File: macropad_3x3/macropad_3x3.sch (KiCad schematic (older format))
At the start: 36 parts, among them Q1 2N7002, U1 TRRS

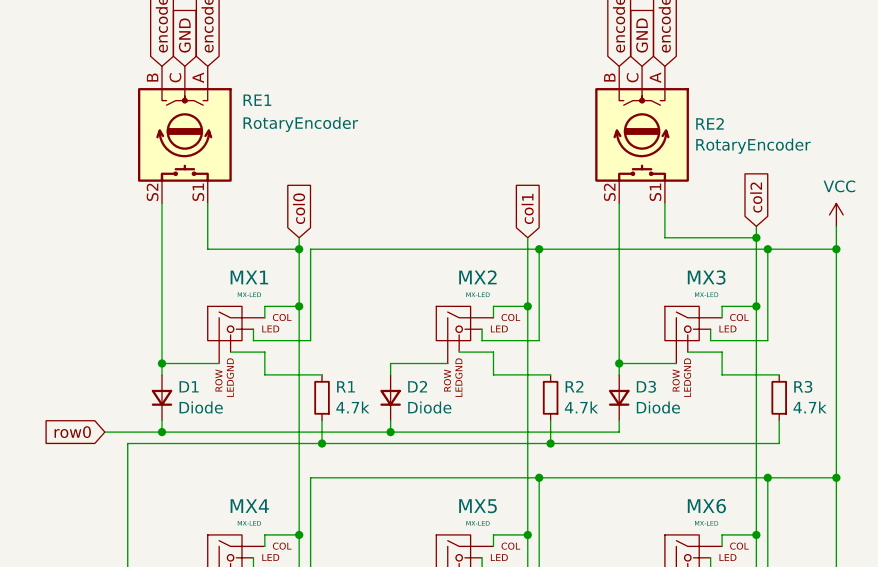
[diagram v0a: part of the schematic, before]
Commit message: 3x3 macropad v2
Updated the 3x3 macropad project to fix the issue with the rotary encoders causing the top corners to always be bridged. Slightly moved the TRRS jack further from the top right switch to give a bit more clearance for the rotary encoder pins.
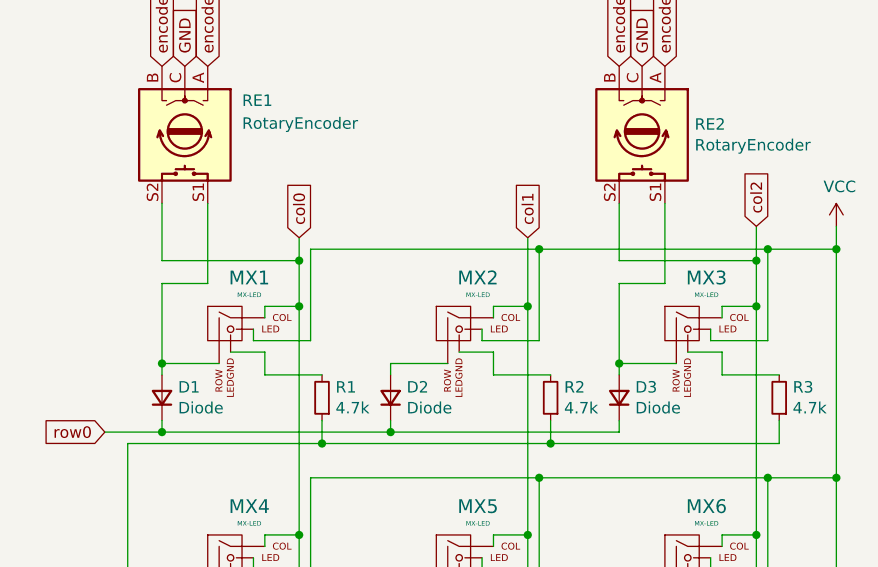
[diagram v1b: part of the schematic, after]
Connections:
- net col0: now also RE1.S2; no longer RE1.S1
- net col2: now also RE2.S2; no longer RE2.S1
- net at D1.2 (A), MX1.2 (ROW): now also RE1.S1; no longer RE1.S2
- net at D3.2 (A), MX3.2 (ROW): now also RE2.S1; no longer RE2.S2
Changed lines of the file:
@@
 	-1   0    0    1
 $EndComp
-Wire Wire Line
-	4250 2000 4250 2700
-Connection ~ 4250 2700
-Wire Wire Line
-	6450 2000 6450 2150
-Wire Wire Line
-	6250 2000 6250 2700
-Connection ~ 6250 2700
 $Comp
 L power:VCC #PWR0111
@@
 Connection ~ 4850 2450
 Wire Wire Line
-	6850 2100 6850 2150
-Wire Wire Line
 	6700 3450 6850 3450
 Wire Wire Line
@@
 	6850 2450 6850 3450
 Connection ~ 6850 2450
-Connection ~ 6850 2150
-Wire Wire Line
-	6850 2150 6850 2450
-Wire Wire Line
-	6450 2150 6850 2150
 Wire Wire Line
 	7200 2100 7200 2200
@@
 Wire Wire Line
 	5250 3000 6250 3000
-Wire Wire Line
-	4450 2000 4450 2200
-Wire Wire Line
-	4850 2200 4850 2450
-Wire Wire Line
-	4850 2150 4850 2200
-Connection ~ 4850 2200
-Wire Wire Line
-	4850 2200 4450 2200
 Wire Wire Line
 	4250 4000 5250 4000
@@
 	1    0    0    -1
 $EndComp
+Wire Wire Line
+	4850 2150 4850 2250
+Wire Wire Line
+	4250 2000 4250 2250
+Wire Wire Line
+	4250 2250 4850 2250
+Connection ~ 4850 2250
+Wire Wire Line
+	4850 2250 4850 2450
+Wire Wire Line
+	4450 2000 4450 2350
+Wire Wire Line
+	4450 2350 4250 2350
+Wire Wire Line
+	4250 2350 4250 2700
+Connection ~ 4250 2700
+Wire Wire Line
+	6850 2100 6850 2250
+Wire Wire Line
+	6250 2000 6250 2250
+Wire Wire Line
+	6250 2250 6850 2250
+Connection ~ 6850 2250
+Wire Wire Line
+	6850 2250 6850 2450
+Wire Wire Line
+	6450 2000 6450 2350
+Wire Wire Line
+	6450 2350 6250 2350
+Wire Wire Line
+	6250 2350 6250 2700
+Connection ~ 6250 2700
 $EndSCHEMATC
